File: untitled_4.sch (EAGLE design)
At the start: 75 parts, among them IC1 LM1875T, IC2 LM1875T, IC3 LM1875T, IC4 LM1875T, J2 power, J3 audio_output, J5 +25v, J6 audio_output, K1 12v, K2 12v

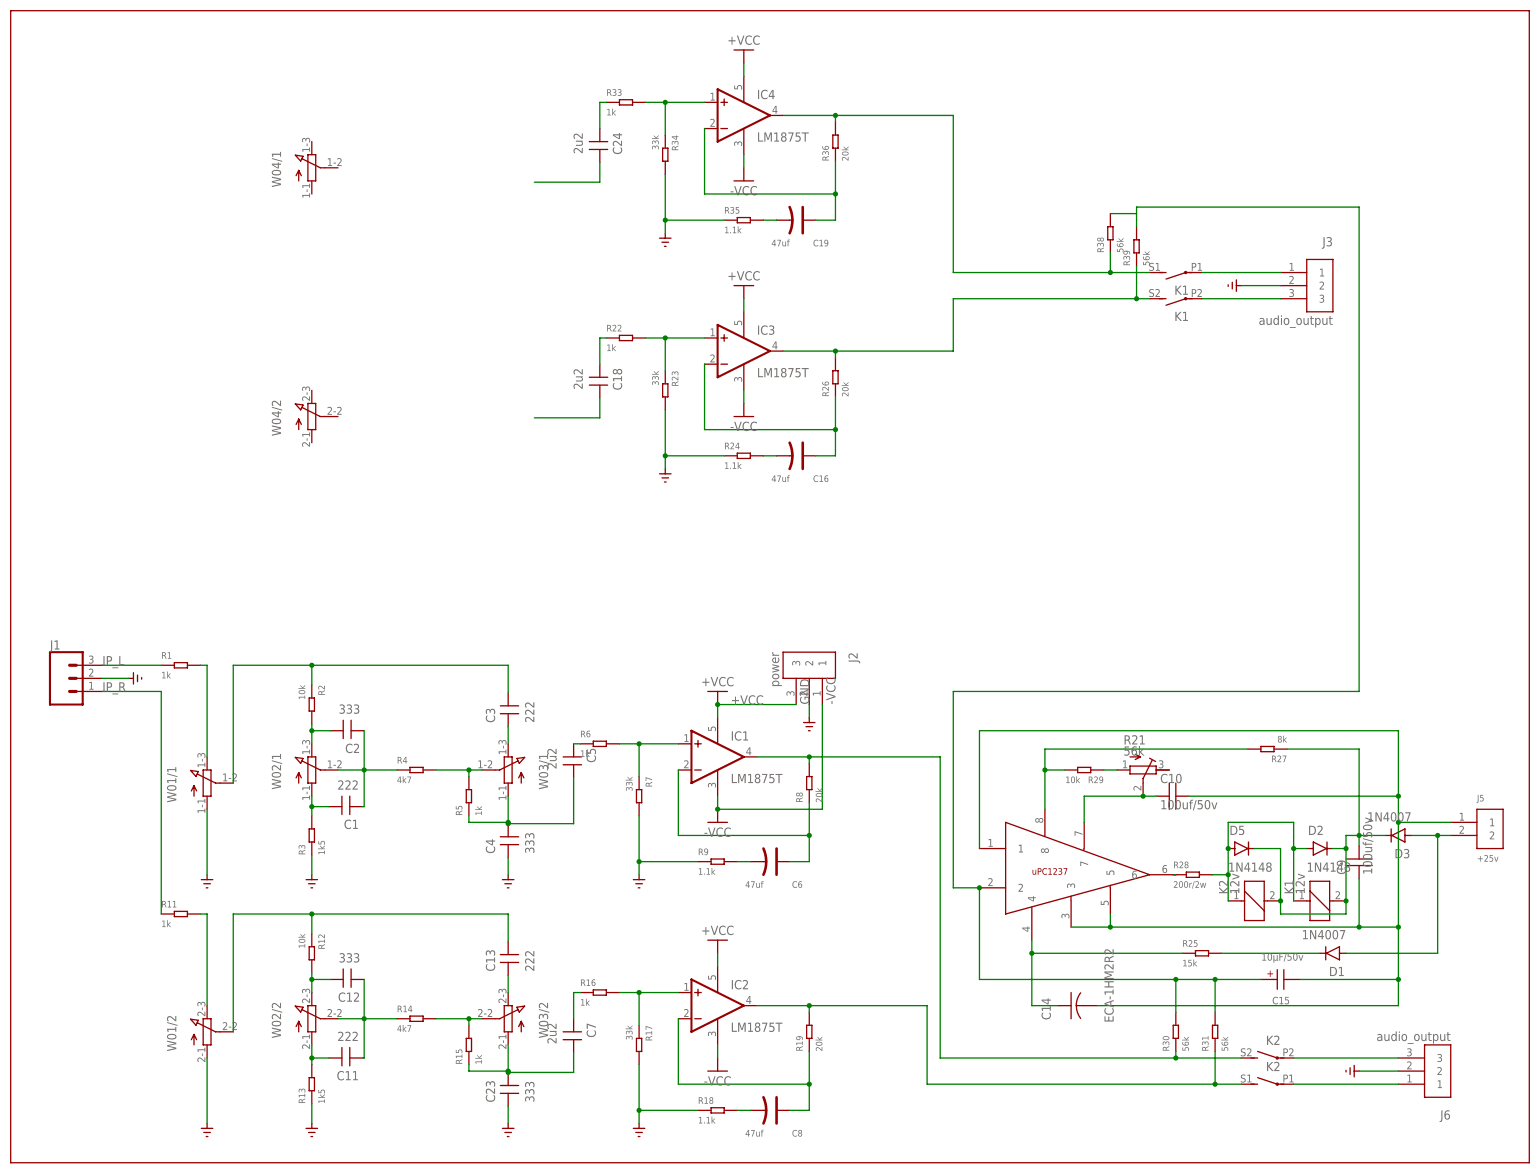
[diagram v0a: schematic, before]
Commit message: 后级放大:更新
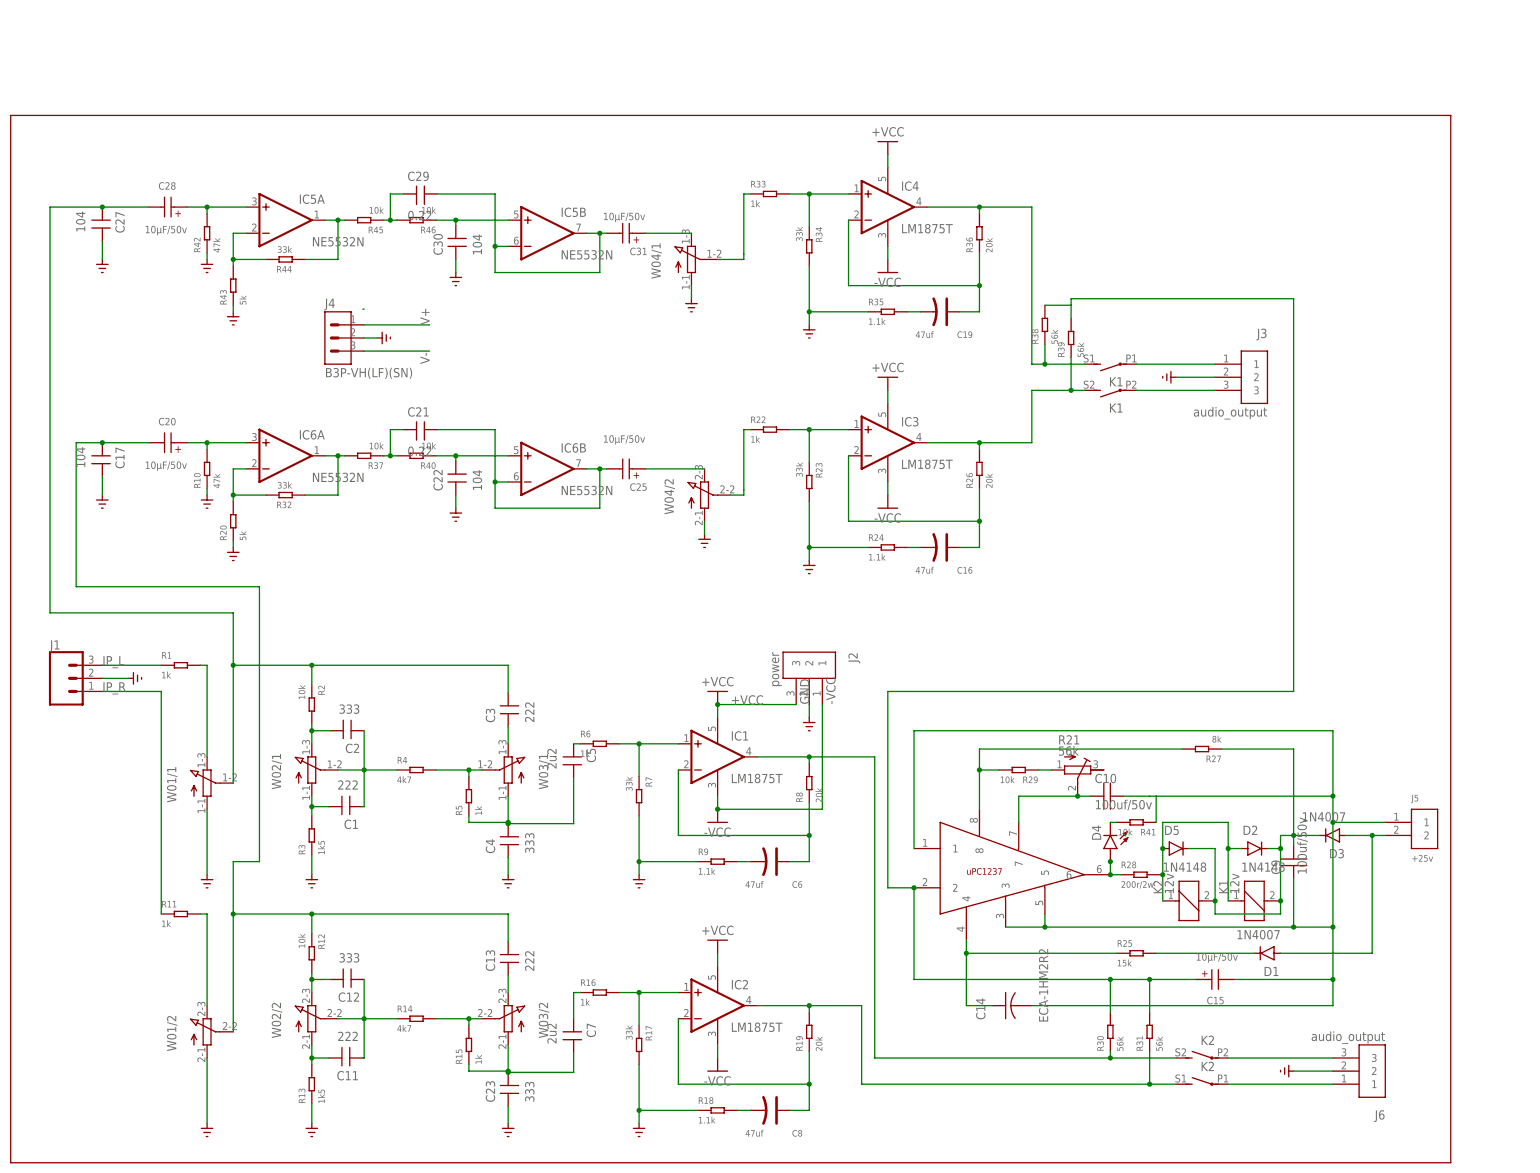
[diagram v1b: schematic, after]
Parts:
- removed C18, C24: 2u2, Audio-Power-amlifier:5.08MM-
- added C17, C22, C27, C30: 104, Audio-Power-amlifier:5.08MM-
- added C20, C25, C28, C31: 10µF/50v, Wurth_Capacitors_WCAP-AT1H:WCAP-AT1H_5X11_860240272001
- added C21, C29: 0.22, Audio-Power-amlifier:5.08MM-
- added D4: (no value), BeagleBone_Blue_R3:BEAGLEBONE_BLUE_LED-3MM-NO_SILK
- added IC5, IC6: NE5532N, linear:NE5532N
- added J4: B3P-VH(LF)(SN), Connectors:B3P-VH(LF)(SN)
- added R10, R42: 47k, OPL_Resistor:DIP-RES-1M-5%-1/4W(PR-D2.3XL6.5MM)
- added R20, R43: 5k, OPL_Resistor:DIP-RES-1M-5%-1/4W(PR-D2.3XL6.5MM)
- added R32, R44: 33k, OPL_Resistor:DIP-RES-1M-5%-1/4W(PR-D2.3XL6.5MM)
- added R37, R40, R41, R45, R46: 10k, OPL_Resistor:DIP-RES-1M-5%-1/4W(PR-D2.3XL6.5MM)
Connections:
- removed net N$53: C24.1, R33.1
- new net N$27: C20.+, IC6A.+IN, R10.2
- new net N$39: IC6A.-IN, R20.2, R32.2
- new net N$55: IC6A.OUT, R32.1, R37.2
- new net N$58: C13.2, C17.1, C20.-, R12.1, W01/2.S
- new net N$59: C21.1, R37.1, R40.2
- new net N$60: C22.2, IC6B.+IN, R40.1
- new net N$61: C21.2, C25.-, IC6B.-IN, IC6B.OUT
- new net N$62: C29.2, C31.-, IC5B.-IN, IC5B.OUT
- new net N$63: IC5A.-IN, R43.2, R44.2
- new net N$64: IC5A.OUT, R44.1, R45.2
- new net N$65: C29.1, R45.1, R46.2
- new net N$66: C30.2, IC5B.+IN, R46.1
- new net N$68: C31.+, W04/1.E
- new net N$69: C25.+, W04/2.E
- new net V+: J4.1
- new net V-: J4.3
- net GND: now also C17.2, C22.1, C27.2, C30.1, J4.2, R10.1, R20.1, R42.1, R43.1, W04/1.A, W04/2.A
- net N$16: now also C27.1, C28.-, C3.2, R2.1, W01/1.S; no longer C13.2, R12.1, W01/2.S
- net N$2: now also D4.C, R41.2; no longer C3.2, R2.1, W01/1.S
- net N$33: now also R33.1, W04/1.S; no longer C18.2
- net N$37: now also W04/2.S; no longer C18.1
- net N$41: now also D4.A
- net N$49: now also C28.+, IC5A.+IN, R42.2; no longer C24.2
- net N$56: now also R41.1
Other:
- moved on the sheet: C10, C14, C15, C16, C19, C9, D1, D2, D3, D5, IC3, IC4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
